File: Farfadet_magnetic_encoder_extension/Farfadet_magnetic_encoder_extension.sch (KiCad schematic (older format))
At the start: 24 parts, among them J1 Conn_02x05_Odd_Even, J2 Conn_01x02, J3 TEST_1P, U1 AS5132-HSS*

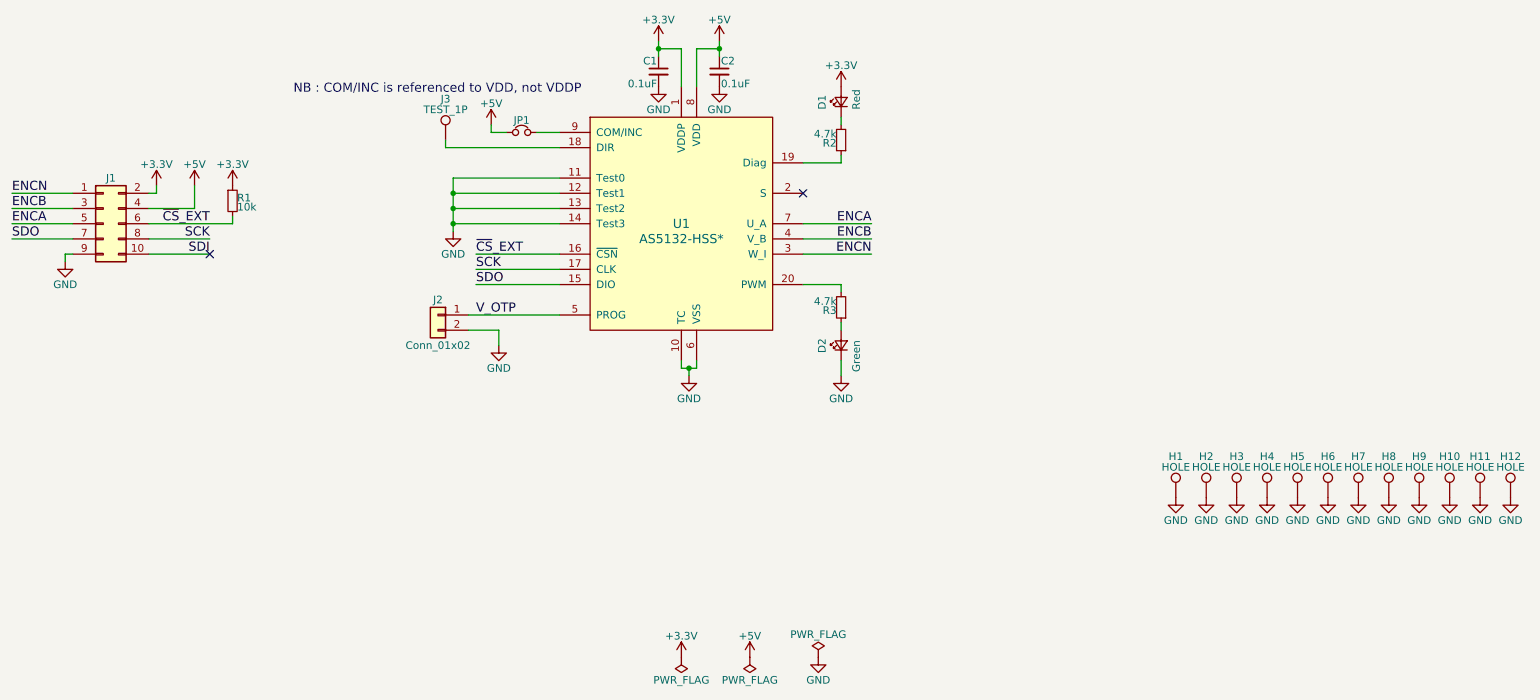
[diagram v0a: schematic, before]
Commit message: Magnetic encoder extension v1.1 : add resistive voltage dividers on 5V signals
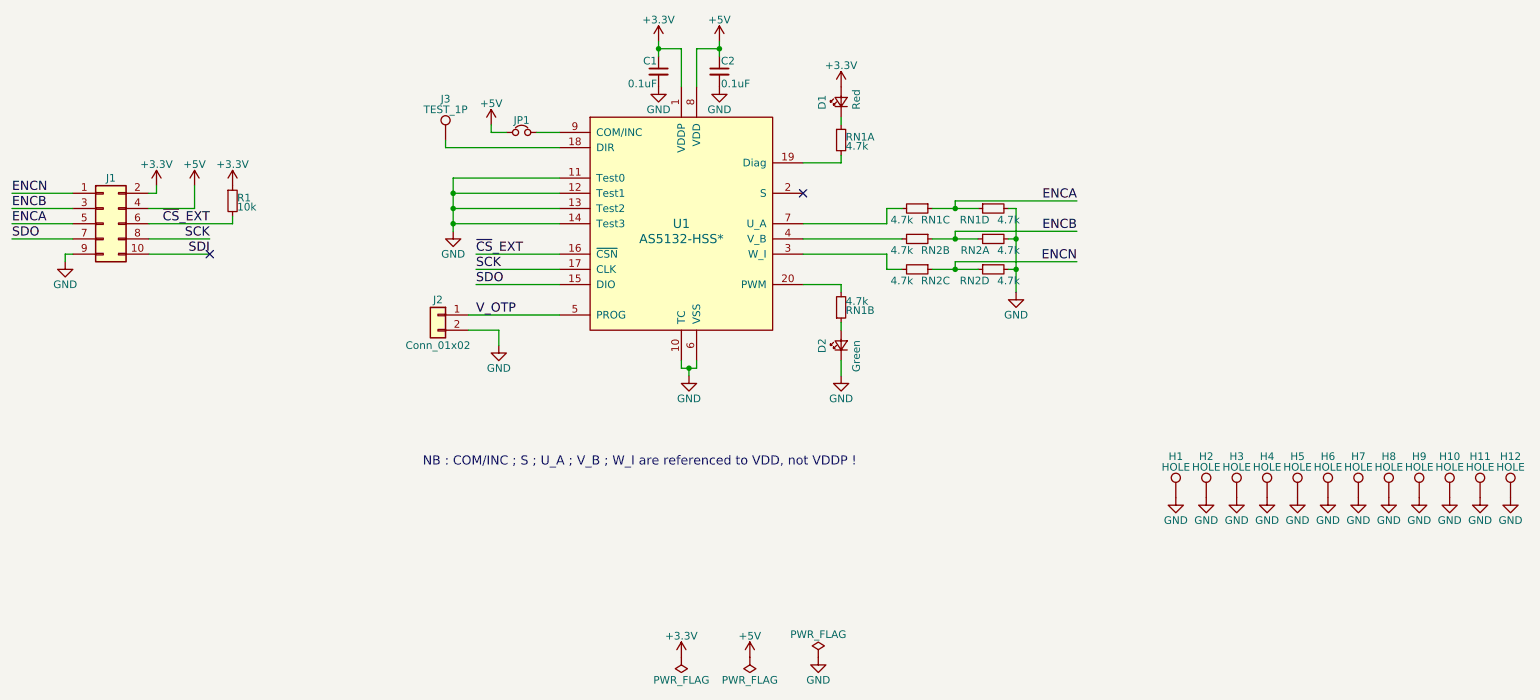
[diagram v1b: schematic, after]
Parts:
- removed R2, R3: 4.7k, Resistors_SMD:R_0603, symbol R_Small
- added RN1, RN2: 4.7k, Resistors_SMD:R_Array_Convex_4x0603, symbol R_Pack04_Unit
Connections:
- net ENCA: now also RN1.3, RN1.4; no longer U1.7 (U_A)
- net ENCB: now also RN2.1, RN2.2; no longer U1.4 (V_B)
- net ENCN: now also RN2.3, RN2.4; no longer U1.3 (W_I)
- net GND: now also RN1.5, RN2.5, RN2.8
- net at U1.19 (Diag): now also RN1.8
- net at U1.20 (PWM): now also RN1.7
- net at D2.2 (A): now also RN1.2
- net at D1.1 (K): now also RN1.1
- new net: RN2.6, U1.3 (W_I)
- new net: RN2.7, U1.4 (V_B)
- new net: RN1.6, U1.7 (U_A)
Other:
- note added: "NB : COM/INC ; S ; U_A ; V_B ; W_I are referenced to VDD, not VDDP !"
- note removed: "NB : COM/INC is referenced to VDD, not VDDP"
